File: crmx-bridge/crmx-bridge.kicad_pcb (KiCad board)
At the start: 4 copper layers, 100.5 x 76.8 mm, 89 parts, among them IC101 ESP32-S3-WROOM-1U-N4R2, J101 Conn_01x18_Pin, J102 NC3FAAH2, J103 TYPEC-304S-ACP16, J104 NC3MAAH, J105 Conn_01x02_Pin, J106 Conn_01x18_Socket, J201 Conn_01x04_Pin, Q101 DMPH4029LFGQ-13, Q102 AO3400A, U101 TIMOTWO, U102 AP63200WU, U103 ISO3088DW, U104 SRV05-4, U105 ISO3088DW, U201 PEC12R-4215F-S0024

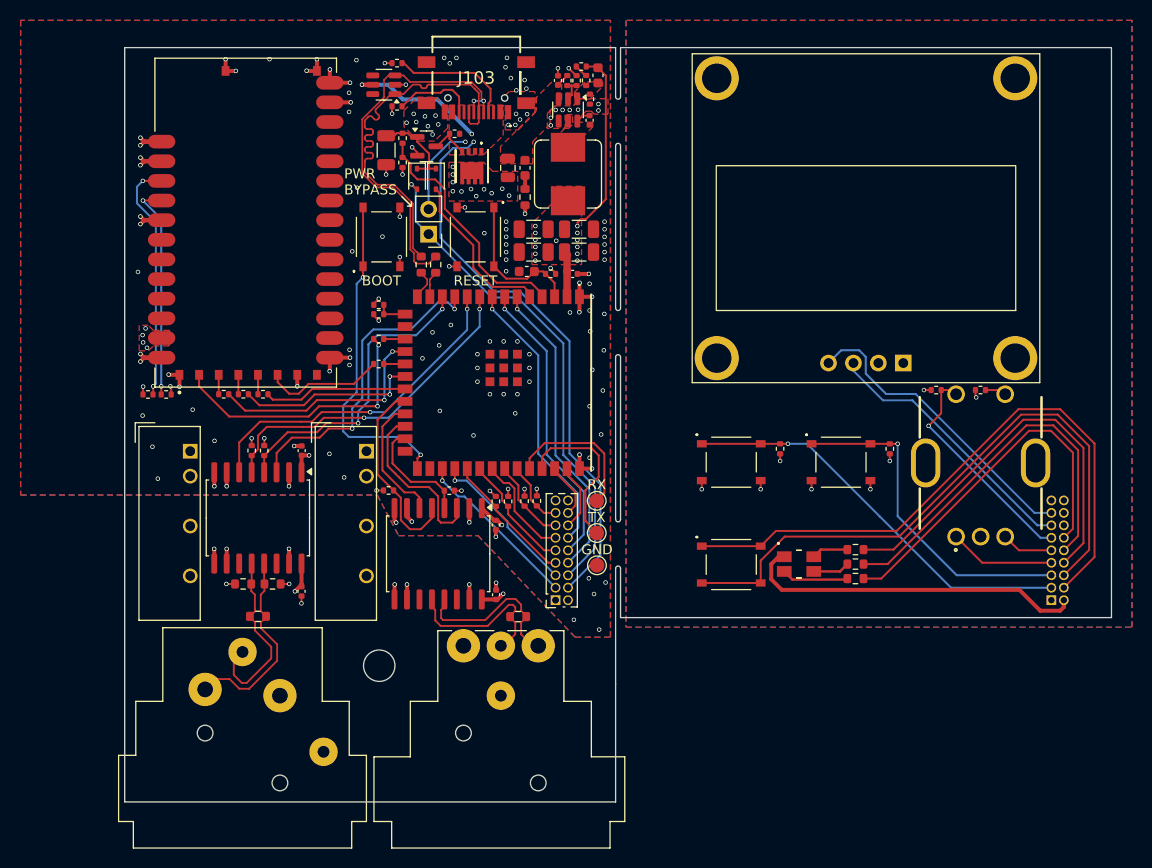
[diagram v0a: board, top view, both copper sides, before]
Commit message: updated to use FPC cable
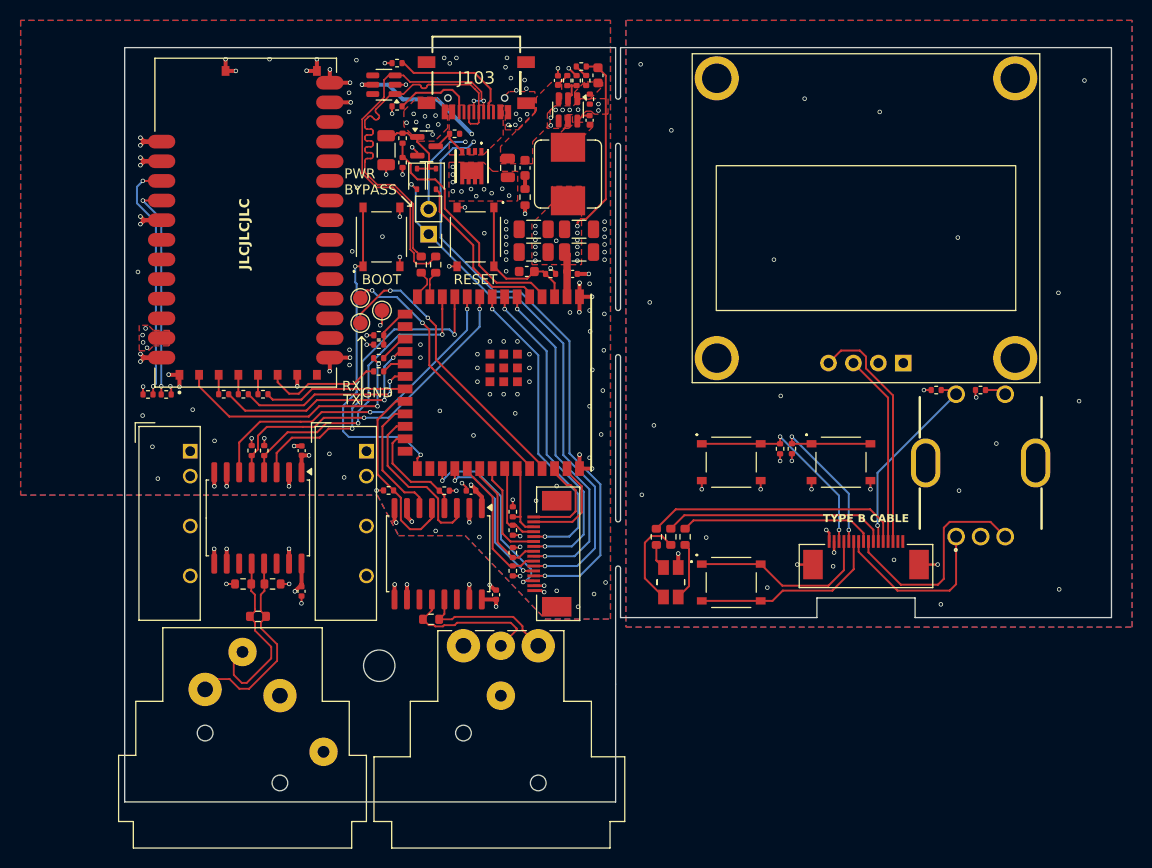
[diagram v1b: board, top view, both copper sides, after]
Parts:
- J101: value Conn_01x18_Pin -> AFC07-S16FCC-00; footprint Connector_PinSocket_1.27mm:PinSocket_2x09_P1.27mm_Vertical -> AFC07-S16FCC-00:AFC07S16FCC00
- J106: value Conn_01x18_Socket -> AFC07-S16FCC-00; footprint Connector_PinHeader_1.27mm:PinHeader_2x09_P1.27mm_Vertical -> AFC07-S16FCC-00:AFC07S16FCC00; moved to F.Cu
- moved J106 50.6 mm to (161.3, 69.3), turned to 90 degrees
- moved TP103 34.0 mm to (143.5, 44.5)
- moved TP102 32.2 mm to (141.3, 45.8)
- moved J101 31.8 mm to (192.8, 70.4), turned to 0 degrees
- moved TP101 31.7 mm to (141.3, 43.2)
- moved R209 20.7 mm to (171.4, 67.6), turned to 90 degrees
- moved R210 19.0 mm to (172.9, 67.6), turned to 90 degrees
- moved R211 17.4 mm to (174.3, 67.6), turned to 90 degrees
- moved D201 13.2 mm to (172.9, 72.2), turned to -90 degrees
- moved R208 9.98 mm to (185.2, 58.6)
- moved R123 8.88 mm to (148.5, 76.0)
- moved R113 7.28 mm to (156.8, 71.0), turned to 90 degrees
- moved R124 5.24 mm to (156.8, 69.2)
- moved C113 4.32 mm to (152.6, 62.9), turned to 180 degrees
- moved R112 3.19 mm to (156.8, 66.9), turned to 90 degrees
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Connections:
- J101 pad 1: GND -> GND1
- J101 pad 10: /LED_G -> /HMI/LED_G
- J101 pad 11: /ENC1.SW -> /HMI/ENC_SW
- J101 pad 12: /LED_R -> /HMI/LED_R
- J101 pad 13: /OLED_SCL -> /HMI/OLED_SCL
- J101 pad 14: /IO1 -> /HMI/OLED_SDA
- J101 pad 15: /OLED_SDA -> unconnected-(J101-Pad15)
- J101 pad 16: /IO2 -> unconnected-(J101-Pad16)
- J101 pad 2: +3V3 -> /HMI/3V3
- J101 pad 3: /OK_BTN -> /HMI/OK_BTN
- J101 pad 4: /VUSB_IN -> /HMI/PWR_BTN_HI
- J101 pad 5: /BK_BTN -> /HMI/BK_BTN
- J101 pad 6: /PWR_BTN_LO -> /HMI/PWR_BTN_LO
- J101 pad 7: /ENC1.A -> /HMI/ENC_A
- J101 pad 8: /LED_B -> /HMI/LED_B
- J101 pad 9: /ENC1.B -> /HMI/ENC_B
- J106 pad 1: GND1 -> GND
- J106 pad 10: /HMI/LED_G -> /LED_G
- J106 pad 11: /HMI/ENC_SW -> /ENC1.SW
- J106 pad 12: /HMI/LED_R -> /LED_R
- J106 pad 13: /HMI/OLED_SCL -> /OLED_SCL
- J106 pad 14: unconnected-(J106-Pin_14-Pad14) -> /OLED_SDA
- J106 pad 15: /HMI/OLED_SDA -> /IO1
- J106 pad 16: unconnected-(J106-Pin_16-Pad16) -> /IO2
- J106 pad 2: /HMI/3V3 -> +3V3
- J106 pad 3: /HMI/OK_BTN -> /OK_BTN
- J106 pad 4: /HMI/PWR_BTN_HI -> /VUSB_IN
- J106 pad 5: /HMI/BK_BTN -> /BK_BTN
- J106 pad 6: /HMI/PWR_BTN_LO -> /PWR_BTN_LO
- J106 pad 7: /HMI/ENC_A -> /ENC1.A
- J106 pad 8: /HMI/LED_B -> /LED_B
- J106 pad 9: /HMI/ENC_B -> /ENC1.B
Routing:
- net /HMI/PWR_BTN_HI: track 63.2 -> 19.0 mm
- net /HMI/PWR_BTN_LO: track 63.4 -> 19.6 mm
- net /HMI/3V3: track 37.4 -> 4.75 mm, vias 3 -> 5
- net /HMI/LED_B: track 41.6 -> 19.9 mm
- net /HMI/OK_BTN: track 41.7 -> 21.9 mm, vias 1 -> 2
- net /HMI/ENC_B: track 5.28 -> 22.7 mm
- net /HMI/LED_G: track 39.5 -> 23.0 mm
- net /TXD0: track 16.5 -> 30.1 mm, vias 0 -> 2
- net /RXD0: track 14.9 -> 27.5 mm, vias 0 -> 2
- net /HMI/BK_BTN: track 34.3 -> 21.8 mm, vias 1 -> 2
- net /HMI/LED_R: track 37.5 -> 26.4 mm
- net /HMI/OLED_SCL: track 27.5 -> 19.6 mm
- net /HMI/ENC_A: track 10.8 -> 17.7 mm
- net /HMI/OLED_SDA: track 31.1 -> 24.6 mm
- net Net-(D201-GK): track 3.74 -> 9.61 mm
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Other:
- outline, holes or cut-outs redrawn
- board text added: "JLCJLCJLC"
- board text added: "TODO: Check dimensions of XLR ports so they align front faces"
- board text added: "TYPE B CABLE"

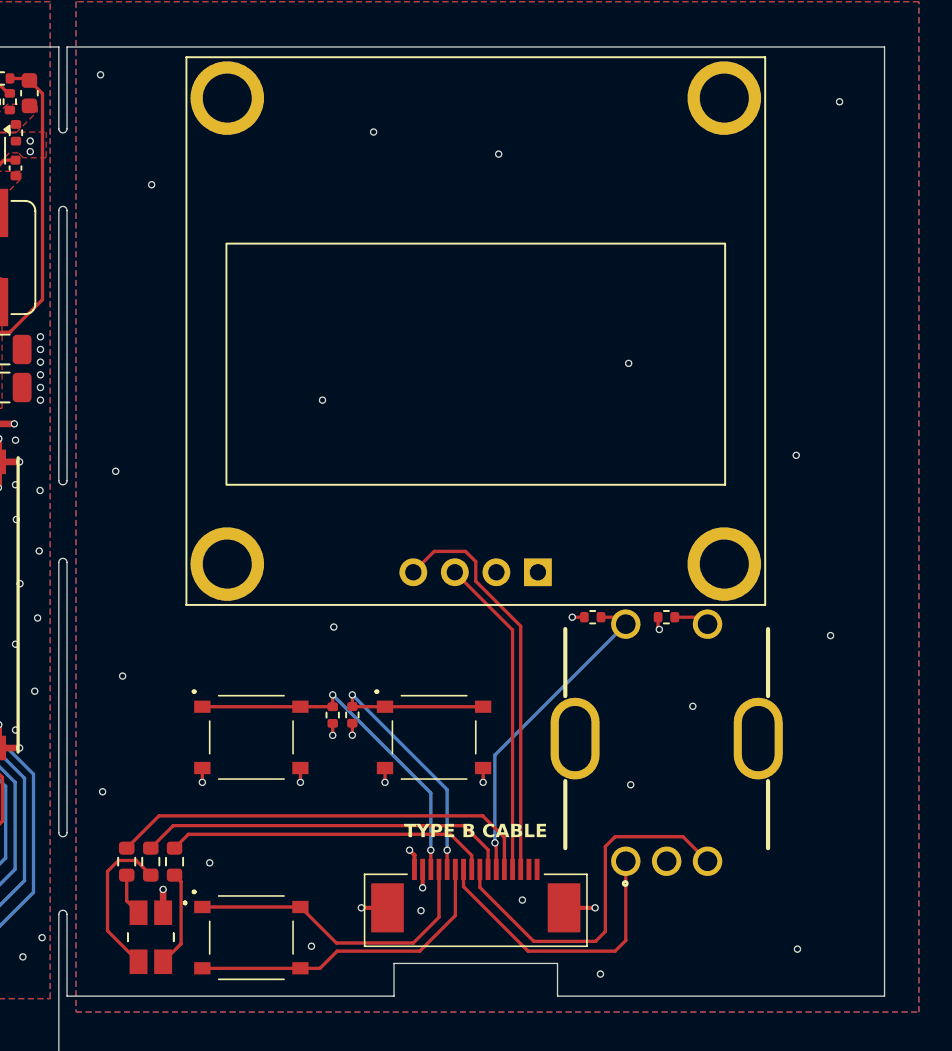
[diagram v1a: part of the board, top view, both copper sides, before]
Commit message: Updated 3d models
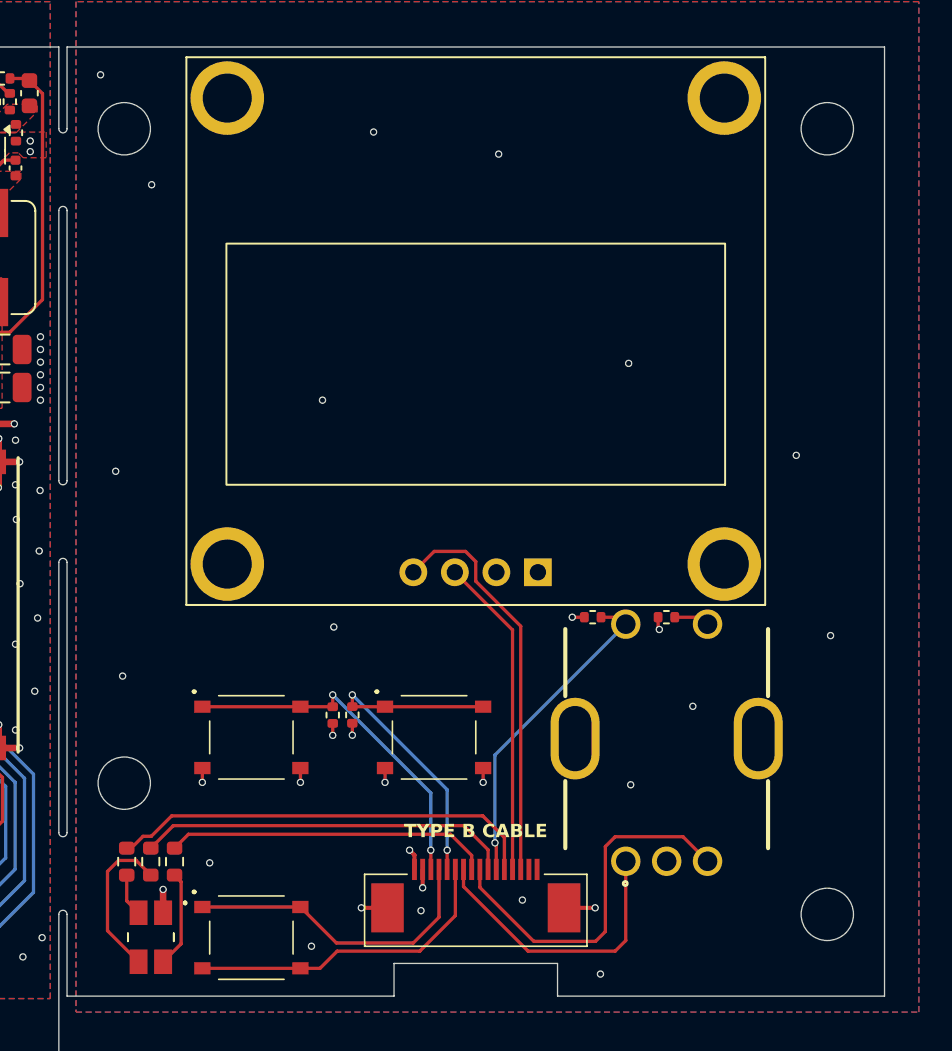
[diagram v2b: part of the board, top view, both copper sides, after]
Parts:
- added H102: MountingHole, MountingHole:MountingHole_3.2mm_M3, F.Cu at (214.3, 70.8)
- added H103: MountingHole, MountingHole:MountingHole_3.2mm_M3, F.Cu at (214.3, 22.8)
- added H104: MountingHole, MountingHole:MountingHole_3.2mm_M3, F.Cu at (171.3, 22.8)
- added H105: MountingHole, MountingHole:MountingHole_3.2mm_M3, F.Cu at (171.3, 62.8)
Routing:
- net GND1: vias 29 -> 26

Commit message: before rearranging
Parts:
- removed PS101, PS102: TEA_1-0505, Converter_DCDC:Converter_DCDC_TRACO_TEA1-xxxxE_THT
- added R125: 10R (1%), Resistor_SMD:R_0603_1608Metric, F.Cu at (131.6, 74.9)
- added U106: TEA1-0505, Converter_DCDC:Converter_DCDC_TRACO_TEA1-xxxx_THT, F.Cu at (193.8, 88.7)
- added U107: TEA1-0505, Converter_DCDC:Converter_DCDC_TRACO_TEA1-xxxx_THT, F.Cu at (186.4, 88.6)
- J103: value TYPEC-304S-ACP16 -> USB_C_Receptacle_USB2.0_16P; footprint LIB_TYPEC-304S-ACP16:TYPEC304SACP16 -> Connector_USB:USB_C_Receptacle_HRO_TYPE-C-31-M-12
- Q101: value DMPH4029LFGQ-13 -> DMP4025SFGQ-13
- R103: value 133R (2%) -> 120R (1%)
- R104, R105: value 562R (2%) -> 560R (1%)
- R132, R137, R138, R139, R140: value 50R -> 49R9
- moved R209 12.1 mm to (183.3, 65.4), turned to 0 degrees
- moved R210 10.5 mm to (183.3, 66.8), turned to 0 degrees
- moved R211 9.00 mm to (183.3, 68.3), turned to 0 degrees
- moved H105 8.02 mm to (171.3, 70.8)
- moved D201 7.94 mm to (179.1, 67.2), turned to 180 degrees
- moved J103 2.60 mm to (153.1, 20.3)
- moved R103 1.08 mm to (130.1, 74.9), turned to 90 degrees
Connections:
- R103 pad 2: /DMX_OUT_N -> Net-(R103-Pad2)
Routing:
- net /HMI/LED_R: track 26.4 -> 13.1 mm
- net /HMI/LED_G: track 23.0 -> 11.8 mm
- net /HMI/LED_B: track 19.9 -> 10.8 mm
- net /VUSB_IN: track 84.0 -> 86.6 mm
- net Net-(R103-Pad2): track 0.00 -> 1.47 mm
- net /USB_DP: track 41.5 -> 40.1 mm
- net Net-(D201-GK): track 9.61 -> 8.96 mm
- net GND1: vias 26 -> 25
- net GND: vias 151 -> 150
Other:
- board text added: "JLCJLCJLCJLC"
- board text removed: "JLCJLCJLC"
- board text removed: "TODO: Check dimensions of XLR ports so they align front faces"
